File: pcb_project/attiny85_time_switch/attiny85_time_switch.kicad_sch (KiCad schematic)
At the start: 32 parts, among them J1 Screw_Terminal_01x02, J2 Conn_02x03_Odd_Even, J3 Conn_01x03_Pin, J4 Screw_Terminal_01x02, J5 Conn_01x03_Pin, J6 Conn_01x03_Pin, J7 Conn_01x02_Pin, J8 Conn_01x02_Pin, Q1 PMV20XNER, Q2 BSS84AK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

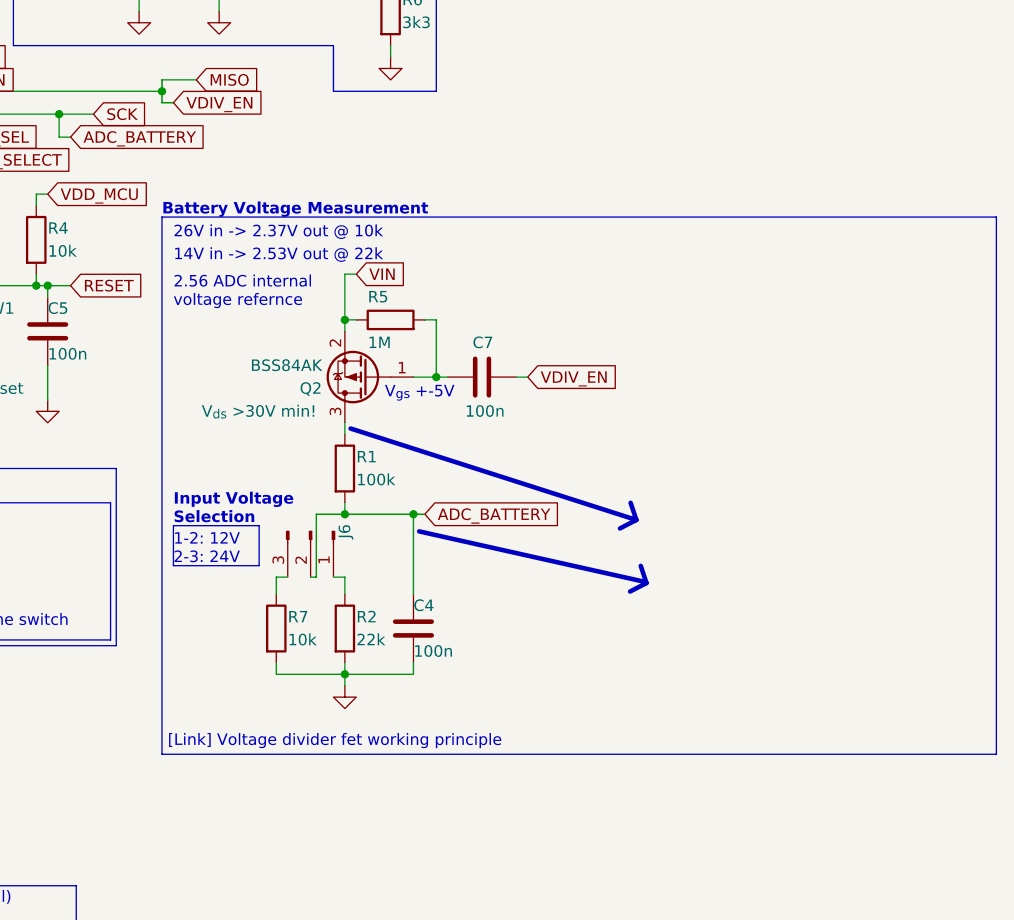
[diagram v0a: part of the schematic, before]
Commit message: 📝 Updated documentation on the zero power measurement link.
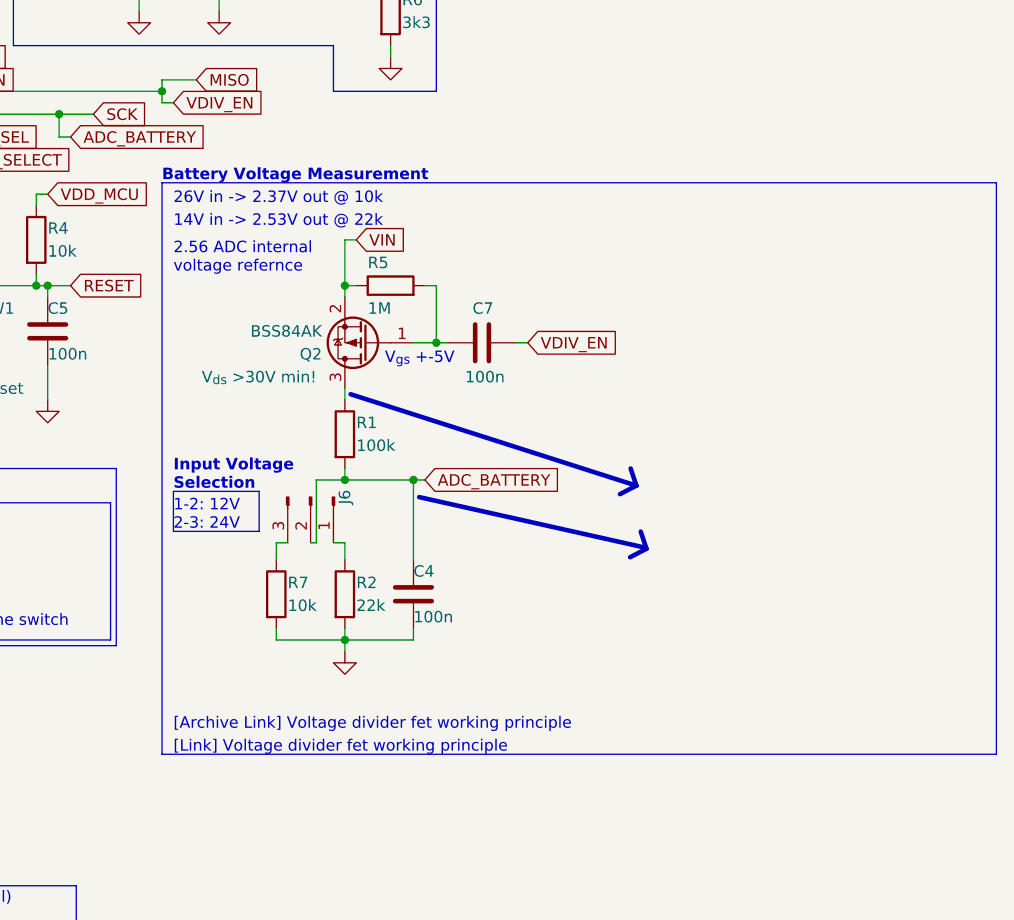
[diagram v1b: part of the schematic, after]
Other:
- note added: "[Archive Link] Voltage divider fet working principle"
- moved on the sheet: C4, C7, J6, Q2, R1, R2, R5, R7
